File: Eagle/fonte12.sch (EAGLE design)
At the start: 13 parts, among them Q1 BC547B

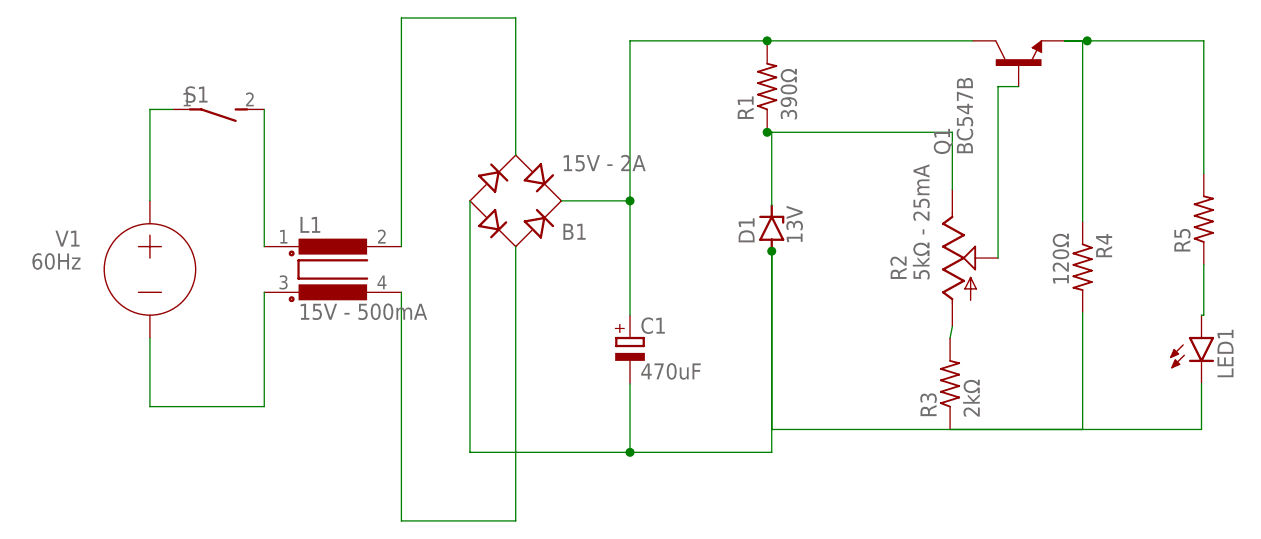
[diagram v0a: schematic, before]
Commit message: Atualização
Atualizei os arquivos do circuito, uma vez que precisei trocar o modelo do potenciômetro.
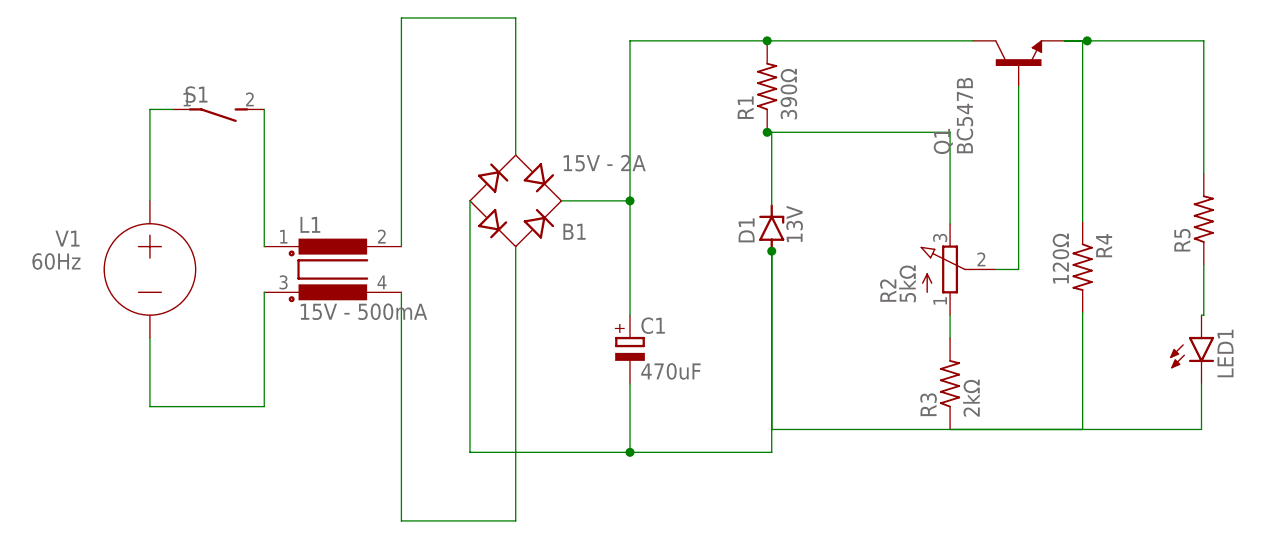
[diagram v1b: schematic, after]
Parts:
- R2: value 5kΩ - 25mA -> 5kΩ; device pot:TRIM_US-B64Y -> pot:3RP/1610N
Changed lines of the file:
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@@
 <part name="Q1" library="transistor-npn" library_urn="urn:adsk.eagle:library:398" deviceset="BC547*" device="" package3d_urn="urn:adsk.eagle:package:28523/2" technology="B"/>
 <part name="S1" library="switch-dil" library_urn="urn:adsk.eagle:library:375" deviceset="DS01E" device="" package3d_urn="urn:adsk.eagle:package:27201/2"/>
-<part name="R2" library="pot" library_urn="urn:adsk.eagle:library:331" deviceset="TRIM_US-" device="B64Y" package3d_urn="urn:adsk.eagle:package:22690/1" value="5kΩ - 25mA"/>
 <part name="L1" library="inductor-nkl" library_urn="urn:adsk.eagle:library:242" deviceset="R1405V" device="B2" package3d_urn="urn:adsk.eagle:package:14869/1" value="15V - 500mA"/>
+<part name="R2" library="pot" library_urn="urn:adsk.eagle:library:331" deviceset="3RP/1610N" device="" package3d_urn="urn:adsk.eagle:package:22726/1" value="5kΩ"/>
 </parts>
 <sheets>
@@
 <attribute name="VALUE" x="-6.35" y="76.2" size="1.778" layer="96" rot="MR180"/>
 </instance>
-<instance part="R2" gate="G$1" x="78.994" y="54.61" smashed="yes">
-<attribute name="NAME" x="73.914" y="52.07" size="1.778" layer="95" rot="R90"/>
-<attribute name="VALUE" x="76.454" y="52.07" size="1.778" layer="96" rot="R90"/>
-</instance>
 <instance part="L1" gate="G$1" x="10.16" y="53.34" smashed="yes">
 <attribute name="NAME" x="6.35" y="57.404" size="1.778" layer="95"/>
 <attribute name="VALUE" x="6.35" y="47.752" size="1.778" layer="96"/>
+</instance>
+<instance part="R2" gate="G$1" x="78.74" y="53.34" smashed="yes">
+<attribute name="NAME" x="72.771" y="49.53" size="1.778" layer="95" rot="R90"/>
+<attribute name="VALUE" x="74.93" y="49.53" size="1.778" layer="96" rot="R90"/>
 </instance>
 </instances>
@@
 <pinref part="R3" gate="G$1" pin="2"/>
 <pinref part="R2" gate="G$1" pin="A"/>
-<wire x1="78.994" y1="46.99" x2="78.74" y2="45.72" width="0.1524" layer="91"/>
+<wire x1="78.74" y1="48.26" x2="78.74" y2="45.72" width="0.1524" layer="91"/>
 </segment>
 </net>
@@
 <wire x1="58.928" y1="68.58" x2="58.42" y2="68.58" width="0.1524" layer="91"/>
 <pinref part="R2" gate="G$1" pin="E"/>
-<wire x1="78.994" y1="62.23" x2="78.994" y2="68.58" width="0.1524" layer="91"/>
-<wire x1="78.994" y1="68.58" x2="58.42" y2="68.58" width="0.1524" layer="91"/>
+<wire x1="78.74" y1="58.42" x2="78.74" y2="68.58" width="0.1524" layer="91"/>
+<wire x1="78.74" y1="68.58" x2="58.42" y2="68.58" width="0.1524" layer="91"/>
 <junction x="58.42" y="68.58"/>
 </segment>
@@
 </segment>
 </net>
-<net name="N$12" class="0">
-<segment>
-<pinref part="Q1" gate="G$1" pin="B"/>
-<pinref part="R2" gate="G$1" pin="S"/>
-<wire x1="86.36" y1="73.66" x2="84.074" y2="73.66" width="0.1524" layer="91"/>
-<wire x1="84.074" y1="73.66" x2="84.074" y2="54.61" width="0.1524" layer="91"/>
-</segment>
-</net>
 <net name="N$11" class="0">
 <segment>
@@
 </segment>
 </net>
+<net name="N$12" class="0">
+<segment>
+<pinref part="R2" gate="G$1" pin="S"/>
+<pinref part="Q1" gate="G$1" pin="B"/>
+<wire x1="83.82" y1="53.34" x2="86.36" y2="53.34" width="0.1524" layer="91"/>
+<wire x1="86.36" y1="53.34" x2="86.36" y2="73.66" width="0.1524" layer="91"/>
+</segment>
+</net>

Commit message: Ajustes pós-apresentação
Adicionou-se a saída do sistema no lugar do R4
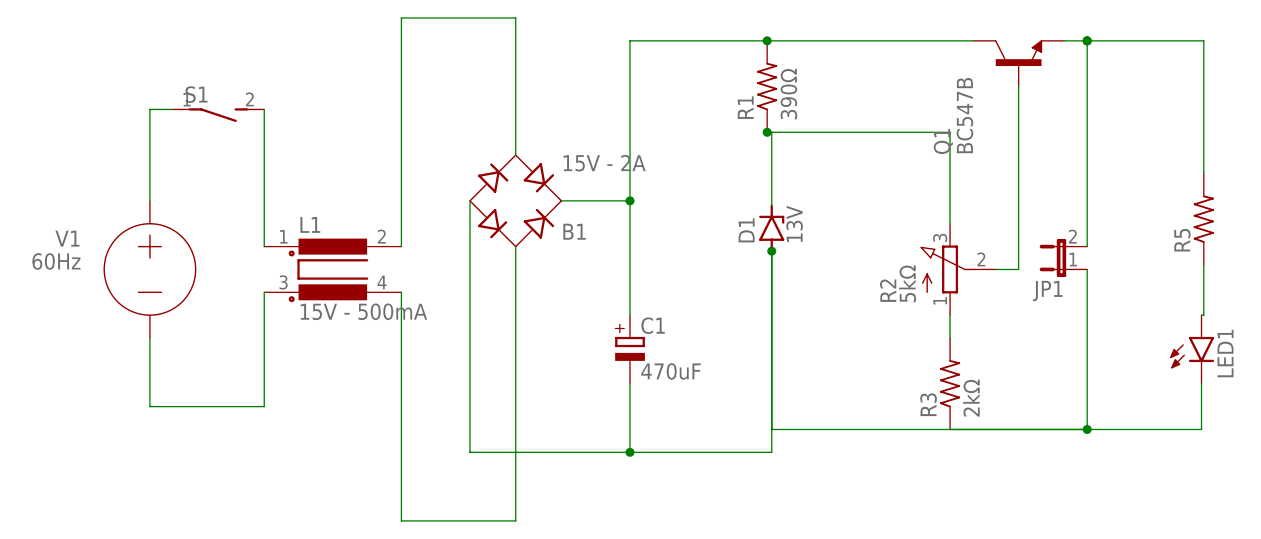
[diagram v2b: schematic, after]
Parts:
- removed R4: 120Ω, rcl:R-US_0309/12
- added JP1: (no value), jumper:JP1E
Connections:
- net N$3: now also JP1.2; no longer R4.1
- net N$6: no longer R4.2
- net N$8: now also JP1.1
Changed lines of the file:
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@@
 <part name="R1" library="rcl" library_urn="urn:adsk.eagle:library:334" deviceset="R-US_" device="0309/12" package3d_urn="urn:adsk.eagle:package:23571/1" value="390Ω"/>
 <part name="R3" library="rcl" library_urn="urn:adsk.eagle:library:334" deviceset="R-US_" device="0309/12" package3d_urn="urn:adsk.eagle:package:23571/1" value="2kΩ"/>
-<part name="R4" library="rcl" library_urn="urn:adsk.eagle:library:334" deviceset="R-US_" device="0309/12" package3d_urn="urn:adsk.eagle:package:23571/1" value="120Ω"/>
 <part name="R5" library="rcl" library_urn="urn:adsk.eagle:library:334" deviceset="R-US_" device="0309/12" package3d_urn="urn:adsk.eagle:package:23571/1"/>
 <part name="LED1" library="led" library_urn="urn:adsk.eagle:library:259" deviceset="LED" device="5MM" package3d_urn="urn:adsk.eagle:package:15799/2"/>
@@
 <part name="L1" library="inductor-nkl" library_urn="urn:adsk.eagle:library:242" deviceset="R1405V" device="B2" package3d_urn="urn:adsk.eagle:package:14869/1" value="15V - 500mA"/>
 <part name="R2" library="pot" library_urn="urn:adsk.eagle:library:331" deviceset="3RP/1610N" device="" package3d_urn="urn:adsk.eagle:package:22726/1" value="5kΩ"/>
+<part name="JP1" library="jumper" library_urn="urn:adsk.eagle:library:252" deviceset="JP1E" device="" package3d_urn="urn:adsk.eagle:package:15455/1"/>
 </parts>
 <sheets>
@@
 <attribute name="VALUE" x="82.042" y="36.83" size="1.778" layer="96" rot="R90"/>
 </instance>
-<instance part="R4" gate="G$1" x="93.472" y="53.594" smashed="yes" rot="R270">
-<attribute name="NAME" x="94.9706" y="57.404" size="1.778" layer="95" rot="R270"/>
-<attribute name="VALUE" x="90.17" y="57.404" size="1.778" layer="96" rot="R270"/>
-</instance>
 <instance part="R5" gate="G$1" x="106.934" y="58.928" smashed="yes" rot="R90">
 <attribute name="NAME" x="105.4354" y="55.118" size="1.778" layer="95" rot="R90"/>
@@
 <attribute name="NAME" x="72.771" y="49.53" size="1.778" layer="95" rot="R90"/>
 <attribute name="VALUE" x="74.93" y="49.53" size="1.778" layer="96" rot="R90"/>
+</instance>
+<instance part="JP1" gate="A" x="91.44" y="53.34" smashed="yes" rot="R90">
+<attribute name="NAME" x="91.44" y="52.07" size="1.778" layer="95" rot="R180"/>
+<attribute name="VALUE" x="91.44" y="59.055" size="1.778" layer="96" rot="R180"/>
 </instance>
 </instances>
@@
 <pinref part="LED1" gate="G$1" pin="C"/>
 <wire x1="106.68" y1="40.64" x2="106.68" y2="35.56" width="0.1524" layer="91"/>
-<wire x1="106.68" y1="35.56" x2="58.928" y2="35.56" width="0.1524" layer="91"/>
+<wire x1="106.68" y1="35.56" x2="93.98" y2="35.56" width="0.1524" layer="91"/>
+<wire x1="93.98" y1="35.56" x2="58.928" y2="35.56" width="0.1524" layer="91"/>
 <wire x1="58.928" y1="35.56" x2="58.928" y2="55.372" width="0.1524" layer="91"/>
 <junction x="58.928" y="55.372"/>
+<pinref part="JP1" gate="A" pin="1"/>
+<wire x1="93.98" y1="53.34" x2="93.98" y2="35.56" width="0.1524" layer="91"/>
+<junction x="93.98" y="35.56"/>
 </segment>
 </net>
@@
 <segment>
 <pinref part="Q1" gate="G$1" pin="E"/>
-<pinref part="R4" gate="G$1" pin="1"/>
-<wire x1="91.44" y1="78.74" x2="93.472" y2="78.74" width="0.1524" layer="91"/>
-<wire x1="93.472" y1="78.74" x2="93.472" y2="58.674" width="0.1524" layer="91"/>
 <pinref part="R5" gate="G$1" pin="2"/>
-<wire x1="91.44" y1="78.74" x2="106.934" y2="78.74" width="0.1524" layer="91"/>
+<wire x1="91.44" y1="78.74" x2="93.98" y2="78.74" width="0.1524" layer="91"/>
+<wire x1="93.98" y1="78.74" x2="106.934" y2="78.74" width="0.1524" layer="91"/>
 <wire x1="106.934" y1="78.74" x2="106.934" y2="64.008" width="0.1524" layer="91"/>
+<pinref part="JP1" gate="A" pin="2"/>
+<wire x1="93.98" y1="78.74" x2="93.98" y2="55.88" width="0.1524" layer="91"/>
 <junction x="93.98" y="78.74"/>
 </segment>
@@
 <net name="N$6" class="0">
 <segment>
-<pinref part="R4" gate="G$1" pin="2"/>
 <pinref part="R3" gate="G$1" pin="1"/>
-<wire x1="93.472" y1="48.514" x2="93.472" y2="35.56" width="0.1524" layer="91"/>
 <wire x1="93.472" y1="35.56" x2="78.74" y2="35.56" width="0.1524" layer="91"/>
 </segment>
@@
 </segment>
 </net>
+<net name="N$14" class="0">
+<segment>
+<junction x="93.98" y="78.74"/>
+</segment>
+</net>
